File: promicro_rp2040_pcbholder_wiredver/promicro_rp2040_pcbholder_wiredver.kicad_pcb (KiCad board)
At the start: 2 copper layers, 117.8 x 39.2 mm, 14 parts, among them J1 Conn_01x08_Pin, J2 Conn_01x08_Pin, J3 Conn_01x08_Pin, J4 Conn_01x08_Pin, U1 RP2040_Pro_Micro, U2 TRRS, U3 RP2040_Pro_Micro, U4 TRRS

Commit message: schematic naming
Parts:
- moved J3 0.58 mm to (173.6, 91.5)
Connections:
- J1 pad 1: Col1 -> RCol1
- J1 pad 2: Col2 -> RCol2
- J1 pad 3: Col3 -> RCol3
- J1 pad 4: Col4 -> RCol4
- J1 pad 5: Col5 -> RCol5
- J1 pad 6: Col6 -> RCol6
- J1 pad 7: Col7 -> RCol7
- J1 pad 8: Col8 -> RCol8
- J2 pad 1: Row1 -> RRow1
- J2 pad 2: Row2 -> RRow2
- J2 pad 3: Row3 -> RRow3
- J2 pad 4: Row4 -> RRow4
- J2 pad 5: Row5 -> RRow5
- J2 pad 6: Row6 -> RRow6
- J2 pad 7: Row7 -> RRow7
- J2 pad 8: Row8 -> RRow8
- J3 pad 1: RCol1 -> LCol1
- J3 pad 2: RCol2 -> LCol2
- J3 pad 3: RCol3 -> LCol3
- J3 pad 4: RCol4 -> LCol4
- J3 pad 5: RCol5 -> LCol5
- J3 pad 6: RCol6 -> LCol6
- J3 pad 7: RCol7 -> LCol7
- J3 pad 8: RCol8 -> LCol8
- J4 pad 1: RRow1 -> LRow1
- J4 pad 2: RRow2 -> LRow2
- J4 pad 3: RRow3 -> LRow3
- J4 pad 4: RRow4 -> LRow4
- J4 pad 5: RRow5 -> LRow5
- J4 pad 6: RRow6 -> LRow6
- J4 pad 7: RRow7 -> LRow7
- J4 pad 8: RRow8 -> LRow8
- U1 pad 10: Col5 -> RCol5
- U1 pad 11: Col6 -> RCol6
- U1 pad 12: Col7 -> RCol7
- U1 pad 13: Col8 -> RCol8
- U1 pad 19: Row8 -> RRow8
- U1 pad 2: LData -> RData
- U1 pad 20: Row7 -> RRow7
- U1 pad 21: Row6 -> RRow6
- U1 pad 22: Row5 -> RRow5
- U1 pad 23: Row4 -> RRow4
- U1 pad 24: Row3 -> RRow3
- U1 pad 25: Row2 -> RRow2
- U1 pad 26: Row1 -> RRow1
- U1 pad 27: LVCC -> RVCC
- U1 pad 5: LGND -> RGND
- U1 pad 6: Col1 -> RCol1
- U1 pad 7: Col2 -> RCol2
- U1 pad 8: Col3 -> RCol3
- U1 pad 9: Col4 -> RCol4
- U2 pad 1: LGND -> RGND
- U2 pad 2: LVCC -> RVCC
- U2 pad 4: LData -> RData
- U3 pad 10: RCol5 -> LCol5
- U3 pad 11: RCol6 -> LCol6
- U3 pad 12: RCol7 -> LCol7
- U3 pad 13: RCol8 -> LCol8
- U3 pad 19: RRow8 -> LRow8
- U3 pad 2: RData -> LData
- U3 pad 20: RRow7 -> LRow7
- U3 pad 21: RRow6 -> LRow6
- U3 pad 22: RRow5 -> LRow5
- U3 pad 23: RRow4 -> LRow4
- U3 pad 24: RRow3 -> LRow3
- U3 pad 25: RRow2 -> LRow2
- U3 pad 26: RRow1 -> LRow1
- U3 pad 27: RVCC -> LVCC
- U3 pad 29: RGND -> LGND
- U3 pad 6: RCol1 -> LCol1
- U3 pad 7: RCol2 -> LCol2
- U3 pad 8: RCol3 -> LCol3
- U3 pad 9: RCol4 -> LCol4
- U4 pad 1: RGND -> LGND
- U4 pad 2: RVCC -> LVCC
- U4 pad 4: RData -> LData
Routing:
- net RCol7: track 0.00 -> 23.7 mm
- net Col7: track 23.7 -> 0.00 mm
- net LRow7: track 0.00 -> 23.1 mm
- net LRow5: track 0.00 -> 23.1 mm
- net LRow3: track 0.00 -> 23.1 mm
- net LRow1: track 0.00 -> 23.1 mm
- net LRow8: track 0.00 -> 23.1 mm
- net LRow4: track 0.00 -> 23.1 mm
- net LRow2: track 0.00 -> 23.1 mm
- net LRow6: track 0.00 -> 23.1 mm
- net RCol8: track 0.00 -> 22.7 mm
- net RCol5: track 0.00 -> 22.7 mm
- net RCol3: track 0.00 -> 22.7 mm
- net RCol1: track 0.00 -> 22.7 mm
- net Col8: track 22.7 -> 0.00 mm
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
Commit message: initial design done. Ordered for testing
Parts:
- removed the ? at (169.5, 75.0)
- removed the ? at (90.0, 74.2)
- added ?: , #footprint:M1.4_tapping_Hole_rev2, F.Cu at (185.0, 77.6)
- added ?: , #footprint:M1.4_tapping_Hole_rev2, F.Cu at (100.3, 74.9)
- J1, J2, J3, J4: footprint Connector_PinHeader_2.54mm:PinHeader_1x08_P2.54mm_Vertical -> #footprint:PinHeader_1x08_P2.54mm_Vertical_rev2
- moved U4 1.40 mm to (173.4, 74.7)
- moved U2 1.25 mm to (113.6, 73.8)
- moved U3 0.62 mm to (186.8, 91.8)
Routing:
- net LVCC: track 7.87 -> 10.7 mm
- net LGND: track 8.30 -> 7.05 mm
- net RCol8: track 22.7 -> 23.6 mm
- net LData: track 23.4 -> 24.3 mm
- net LCol8: track 21.7 -> 22.5 mm
- net RVCC: track 19.2 -> 19.8 mm
- net LRow3: track 23.1 -> 22.5 mm
- net LRow4: track 23.1 -> 22.5 mm
- net LRow2: track 23.1 -> 22.5 mm
- net LRow5: track 23.1 -> 22.5 mm
- net LRow1: track 23.1 -> 22.5 mm
- net LRow6: track 23.1 -> 22.5 mm
- net LCol4: track 21.7 -> 22.3 mm
- net LCol6: track 21.7 -> 22.3 mm
- net LCol5: track 21.7 -> 22.3 mm
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
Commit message: tested working. Swap left side pcb's rows and cols wire holes
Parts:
- moved J3 26.3 mm to (199.9, 92.3)
- moved J4 26.3 mm to (173.6, 91.5)
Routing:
- net LRow7: track 23.6 -> 7.02 mm
- net LRow8: track 23.4 -> 7.02 mm
- net LRow1: track 22.5 -> 7.02 mm
- net LRow6: track 22.5 -> 7.02 mm
- net LRow5: track 22.5 -> 7.02 mm
- net LRow4: track 22.5 -> 7.02 mm
- net LRow2: track 22.5 -> 7.02 mm
- net LRow3: track 22.5 -> 7.02 mm
- net LCol7: track 22.3 -> 7.25 mm
- net LCol8: track 22.5 -> 7.72 mm
- net LCol5: track 22.3 -> 7.97 mm
- net LCol4: track 22.3 -> 7.99 mm
- net LCol3: track 22.3 -> 8.00 mm
- net LCol2: track 22.3 -> 8.02 mm
- net LCol6: track 22.3 -> 8.03 mm
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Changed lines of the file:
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@@
 	(footprint "#footprint:PinHeader_1x08_P2.54mm_Vertical_rev2"
 		(layer "B.Cu")
-		(at 199.852501 92.30625 180)
+		(at 173.602501 91.47625 180)
 		(descr "Through hole straight pin header, 1x08, 2.54mm pitch, single row")
 		(tags "Through hole pin header THT 1x08 2.54mm single row")
@@
 	(footprint "#footprint:PinHeader_1x08_P2.54mm_Vertical_rev2"
 		(layer "B.Cu")
-		(at 173.602501 91.47625 180)
+		(at 199.852501 92.30625 180)
 		(descr "Through hole straight pin header, 1x08, 2.54mm pitch, single row")
 		(tags "Through hole pin header THT 1x08 2.54mm single row")
@@
 	)
 	(gr_text "Rows"
-		(at 201.852501 90.55625 0)
+		(at 175.592501 89.80625 0)
 		(layer "B.SilkS")
 		(effects
@@
 	)
 	(gr_text "Cols"
-		(at 176.102501 89.80625 0)
+		(at 201.592501 90.73625 0)
 		(layer "B.SilkS")
 		(effects
@@
 	)
 	(gr_text "Rows"
-		(at 197.852501 90.55625 0)
+		(at 171.592501 89.80625 0)
 		(layer "F.SilkS")
 		(effects
@@
 	)
 	(gr_text "Cols"
-		(at 172.602501 89.80625 0)
+		(at 198.092501 90.73625 0)
 		(layer "F.SilkS")
 		(effects
@@
 	)
 	(segment
-		(start 173.602501 106.71625)
-		(end 175.862501 104.45625)
-		(width 0.2)
-		(layer "F.Cu")
-		(net 6)
-	)
-	(segment
-		(start 175.862501 104.45625)
-		(end 193.142501 104.45625)
+		(start 199.852501 107.54625)
+		(end 198.752501 107.54625)
 		(width 0.2)
 		(layer "F.Cu")
@@
 	)
 	(segment
-		(start 193.142501 104.45625)
+		(start 198.752501 107.54625)
 		(end 194.402501 103.19625)
 		(width 0.2)
@@
 	)
 	(segment
-		(start 175.932501 99.30625)
-		(end 193.212501 99.30625)
+		(start 198.752501 102.46625)
+		(end 194.402501 98.11625)
 		(width 0.2)
 		(layer "F.Cu")
@@
 	)
 	(segment
-		(start 173.602501 101.63625)
-		(end 175.932501 99.30625)
+		(start 199.852501 102.46625)
+		(end 198.752501 102.46625)
 		(width 0.2)
 		(layer "F.Cu")
@@
 	)
 	(segment
-		(start 193.212501 99.30625)
-		(end 194.402501 98.11625)
+		(start 199.852501 102.46625)
+		(end 199.342501 101.95625)
 		(width 0.2)
-		(layer "F.Cu")
+		(layer "B.Cu")
 		(net 7)
 	)
 	(segment
-		(start 193.142501 91.75625)
-		(end 194.402501 90.49625)
+		(start 199.852501 94.84625)
+		(end 198.752501 94.84625)
 		(width 0.2)
 		(layer "F.Cu")
@@
 	)
 	(segment
-		(start 173.602501 94.01625)
-		(end 175.862501 91.75625)
+		(start 198.752501 94.84625)
+		(end 194.402501 90.49625)
 		(width 0.2)
 		(layer "F.Cu")
@@
 	)
 	(segment
-		(start 175.862501 91.75625)
-		(end 193.142501 91.75625)
+		(start 199.852501 94.84625)
+		(end 199.312501 94.30625)
 		(width 0.2)
-		(layer "F.Cu")
+		(layer "B.Cu")
 		(net 11)
 	)
 	(segment
-		(start 193.052501 89.30625)
-		(end 194.402501 87.95625)
+		(start 199.852501 92.30625)
+		(end 198.752501 92.30625)
 		(width 0.2)
 		(layer "F.Cu")
@@
 	)
 	(segment
-		(start 173.602501 91.47625)
-		(end 175.772501 89.30625)
+		(start 198.752501 92.30625)
+		(end 194.402501 87.95625)
 		(width 0.2)
 		(layer "F.Cu")
@@
 	)
 	(segment
-		(start 175.772501 89.30625)
-		(end 193.052501 89.30625)
+		(start 199.852501 92.30625)
+		(end 199.302501 91.75625)
 		(width 0.2)
-		(layer "F.Cu")
+		(layer "B.Cu")
 		(net 12)
 	)
 	(segment
-		(start 191.352501 109.25625)
-		(end 194.402501 106.20625)
+		(start 198.752501 110.08625)
+		(end 194.402501 105.73625)
 		(width 0.2)
 		(layer "F.Cu")
@@
 	)
 	(segment
-		(start 173.602501 109.25625)
-		(end 191.352501 109.25625)
+		(start 199.852501 110.08625)
+		(end 198.752501 110.08625)
 		(width 0.2)
 		(layer "F.Cu")
@@
 	)
 	(segment
-		(start 193.202501 101.85625)
-		(end 194.402501 100.65625)
+		(start 199.852501 105.00625)
+		(end 198.752501 105.00625)
 		(width 0.2)
 		(layer "F.Cu")
@@
 	)
 	(segment
-		(start 173.602501 104.17625)
-		(end 175.922501 101.85625)
+		(start 198.752501 105.00625)
+		(end 194.402501 100.65625)
 		(width 0.2)
 		(layer "F.Cu")
@@
 	)
 	(segment
-		(start 175.922501 101.85625)
-		(end 193.202501 101.85625)
+		(start 199.852501 105.00625)
+		(end 199.302501 104.45625)
 		(width 0.2)
-		(layer "F.Cu")
+		(layer "B.Cu")
 		(net 15)
 	)
 	(segment
-		(start 175.892501 96.80625)
-		(end 193.172501 96.80625)
+		(start 199.852501 99.92625)
+		(end 198.752501 99.92625)
 		(width 0.2)
 		(layer "F.Cu")
@@
 	)
 	(segment
-		(start 193.172501 96.80625)
+		(start 198.752501 99.92625)
 		(end 194.402501 95.57625)
 		(width 0.2)
@@
 	)
 	(segment
-		(start 173.602501 99.09625)
-		(end 175.892501 96.80625)
+		(start 199.852501 99.92625)
+		(end 199.332501 99.40625)
 		(width 0.2)
-		(layer "F.Cu")
+		(layer "B.Cu")
 		(net 16)
 	)
 	(segment
-		(start 173.602501 96.55625)
-		(end 175.902501 94.25625)
-		(width 0.2)
-		(layer "F.Cu")
-		(net 17)
-	)
-	(segment
-		(start 175.902501 94.25625)
-		(end 193.182501 94.25625)
+		(start 199.852501 97.38625)
+		(end 198.752501 97.38625)
 		(width 0.2)
 		(layer "F.Cu")
@@
 	)
 	(segment
-		(start 193.182501 94.25625)
+		(start 198.752501 97.38625)
 		(end 194.402501 93.03625)
 		(width 0.2)
@@
 		(width 0.2)
 		(layer "B.Cu")
-		(net 19)
+		(net 17)
 	)
 	(segment
-		(start 199.322501 96.85625)
-		(end 182.982501 96.85625)
+		(start 173.602501 96.55625)
+		(end 175.642501 96.55625)
 		(width 0.2)
-		(layer "B.Cu")
+		(layer "F.Cu")
 		(net 19)
 	)
 	(segment
-		(start 182.982501 96.85625)
+		(start 175.642501 96.55625)
 		(end 179.162501 93.03625)
 		(width 0.2)
-		(layer "B.Cu")
+		(layer "F.Cu")
 		(net 19)
 	)
 	(segment
-		(start 199.852501 107.54625)
-		(end 181.594606 107.54625)
-		(width 0.2)
-		(layer "B.Cu")
-		(net 21)
-	)
-	(segment
-		(start 181.594606 107.54625)
-		(end 180.402501 106.354145)
-		(width 0.2)
-		(layer "B.Cu")
-		(net 21)
-	)
-	(segment
-		(start 180.402501 106.354145)
-		(end 180.402501 104.43625)
-		(width 0.2)
-		(layer "B.Cu")
-		(net 21)
-	)
-	(segment
-		(start 180.402501 104.43625)
+		(start 175.642501 106.71625)
 		(end 179.162501 103.19625)
 		(width 0.2)
-		(layer "B.Cu")
+		(layer "F.Cu")
 		(net 21)
 	)
 	(segment
-		(start 199.302501 104.45625)
-		(end 182.962501 104.45625)
+		(start 173.602501 106.71625)
+		(end 175.642501 106.71625)
 		(width 0.2)
-		(layer "B.Cu")
-		(net 22)
+		(layer "F.Cu")
+		(net 21)
 	)
 	(segment
-		(start 199.852501 105.00625)
-		(end 199.302501 104.45625)
+		(start 175.642501 104.17625)
+		(end 179.162501 100.65625)
 		(width 0.2)
-		(layer "B.Cu")
+		(layer "F.Cu")
 		(net 22)
 	)
 	(segment
-		(start 182.962501 104.45625)
-		(end 179.162501 100.65625)
+		(start 173.602501 104.17625)
+		(end 175.642501 104.17625)
 		(width 0.2)
-		(layer "B.Cu")
+		(layer "F.Cu")
 		(net 22)
 	)
@@
 	)
 	(segment
-		(start 199.342501 101.95625)
-		(end 183.002501 101.95625)
-		(width 0.2)
-		(layer "B.Cu")
-		(net 26)
-	)
-	(segment
-		(start 183.002501 101.95625)
+		(start 175.642501 101.63625)
 		(end 179.162501 98.11625)
 		(width 0.2)
-		(layer "B.Cu")
+		(layer "F.Cu")
 		(net 26)
 	)
 	(segment
-		(start 199.852501 102.46625)
-		(end 199.342501 101.95625)
+		(start 173.602501 101.63625)
+		(end 175.642501 101.63625)
 		(width 0.2)
-		(layer "B.Cu")
+		(layer "F.Cu")
 		(net 26)
 	)
 	(segment
-		(start 199.312501 94.30625)
-		(end 182.972501 94.30625)
-		(width 0.2)
-		(layer "B.Cu")
-		(net 27)
-	)
-	(segment
-		(start 182.972501 94.30625)
+		(start 175.642501 94.01625)
 		(end 179.162501 90.49625)
 		(width 0.2)
-		(layer "B.Cu")
+		(layer "F.Cu")
 		(net 27)
 	)
 	(segment
-		(start 199.852501 94.84625)
-		(end 199.312501 94.30625)
+		(start 173.602501 94.01625)
+		(end 175.642501 94.01625)
 		(width 0.2)
-		(layer "B.Cu")
+		(layer "F.Cu")
 		(net 27)
 	)
 	(segment
-		(start 181.882501 110.08625)
-		(end 179.162501 107.36625)
-		(width 0.2)
-		(layer "B.Cu")
-		(net 29)
-	)
-	(segment
-		(start 199.852501 110.08625)
-		(end 181.882501 110.08625)
+		(start 173.602501 109.25625)
+		(end 175.642501 109.25625)
 		(width 0.2)
-		(layer "B.Cu")
+		(layer "F.Cu")
 		(net 29)
 	)
 	(segment
-		(start 179.162501 107.36625)
+		(start 175.642501 109.25625)
 		(end 179.162501 105.73625)
 		(width 0.2)
-		(layer "B.Cu")
+		(layer "F.Cu")
 		(net 29)
 	)
 	(segment
-		(start 199.302501 91.75625)
-		(end 182.962501 91.75625)
+		(start 173.602501 91.47625)
+		(end 175.642501 91.47625)
 		(width 0.2)
-		(layer "B.Cu")
+		(layer "F.Cu")
 		(net 30)
 	)
 	(segment
-		(start 182.962501 91.75625)
+		(start 175.642501 91.47625)
 		(end 179.162501 87.95625)
 		(width 0.2)
-		(layer "B.Cu")
-		(net 30)
-	)
-	(segment
-		(start 199.852501 92.30625)
-		(end 199.302501 91.75625)
-		(width 0.2)
-		(layer "B.Cu")
+		(layer "F.Cu")
 		(net 30)
 	)
 	(segment
-		(start 182.992501 99.40625)
+		(start 175.642501 99.09625)
 		(end 179.162501 95.57625)
 		(width 0.2)
-		(layer "B.Cu")
-		(net 31)
-	)
-	(segment
-		(start 199.852501 99.92625)
-		(end 199.332501 99.40625)
-		(width 0.2)
-		(layer "B.Cu")
+		(layer "F.Cu")
 		(net 31)
 	)
 	(segment
-		(start 199.332501 99.40625)
-		(end 182.992501 99.40625)
+		(start 173.602501 99.09625)
+		(end 175.642501 99.09625)
 		(width 0.2)
-		(layer "B.Cu")
+		(layer "F.Cu")
 		(net 31)
 	)

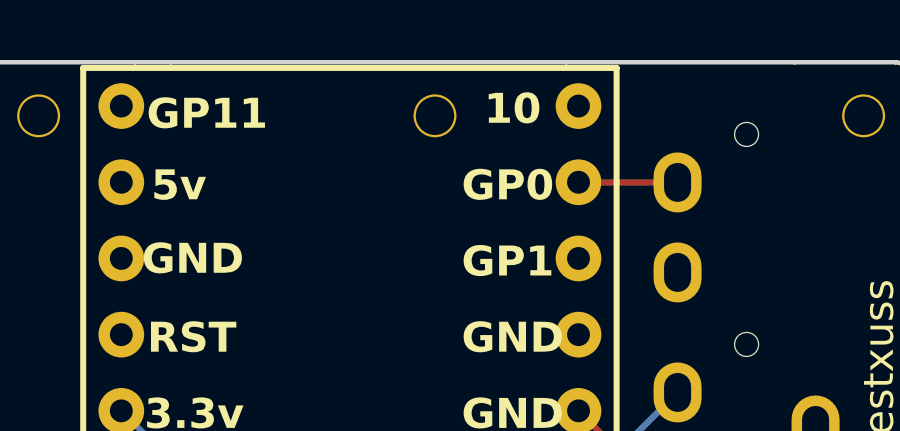
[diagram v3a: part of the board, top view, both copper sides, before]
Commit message: slight change m1.4 right side pcb hole spacing
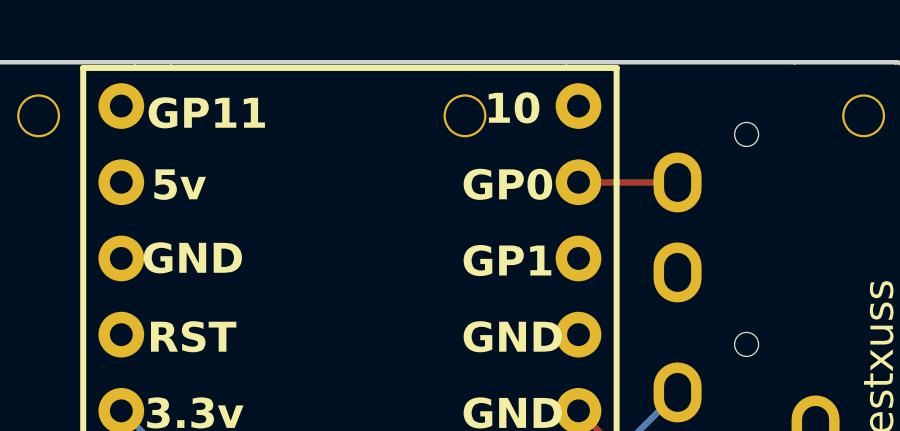
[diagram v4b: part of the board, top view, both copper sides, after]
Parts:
- moved ? 1.00 mm to (104.2, 74.8)
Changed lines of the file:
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@@
 	(footprint "#footprint:M1.4_tapping_Hole_rev2"
 		(layer "F.Cu")
-		(at 103.216326 74.78583 -90)
+		(at 104.216326 74.78583 -90)
 		(descr "Resitance 3 pas")
 		(tags "R")
